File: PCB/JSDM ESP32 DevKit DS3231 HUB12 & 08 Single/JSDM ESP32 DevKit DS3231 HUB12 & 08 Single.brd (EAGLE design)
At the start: 14 parts, among them X1 PSU

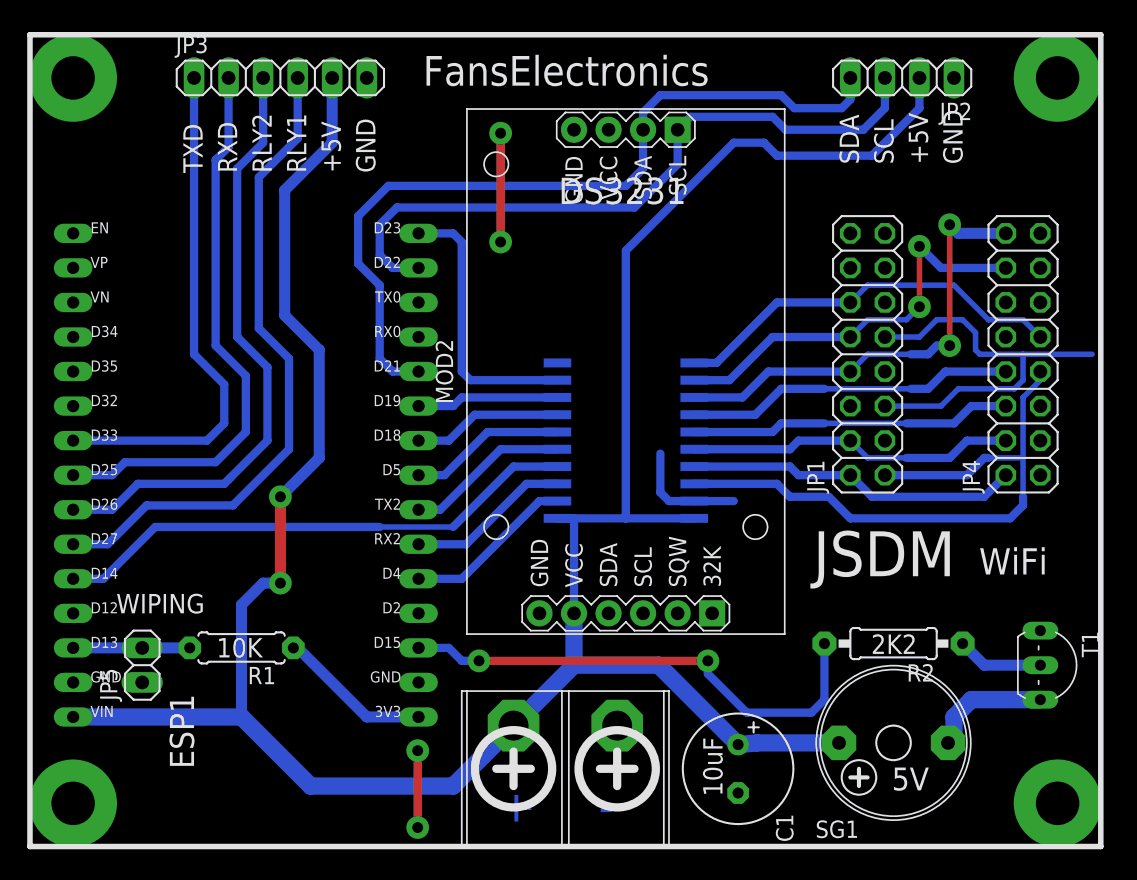
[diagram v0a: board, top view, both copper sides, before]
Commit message: JSDM PCB Single Layer ESP8266 + ESP32
Desain PCB SIngle Layer versi:
- Wemos D1 mini HUB12 + HUB08
- Wemos D1 Mini 3x HUB12
- ESP32 Devkit HUB12 + HUB08
- ESP32 Devkit Mini 3x HUB12
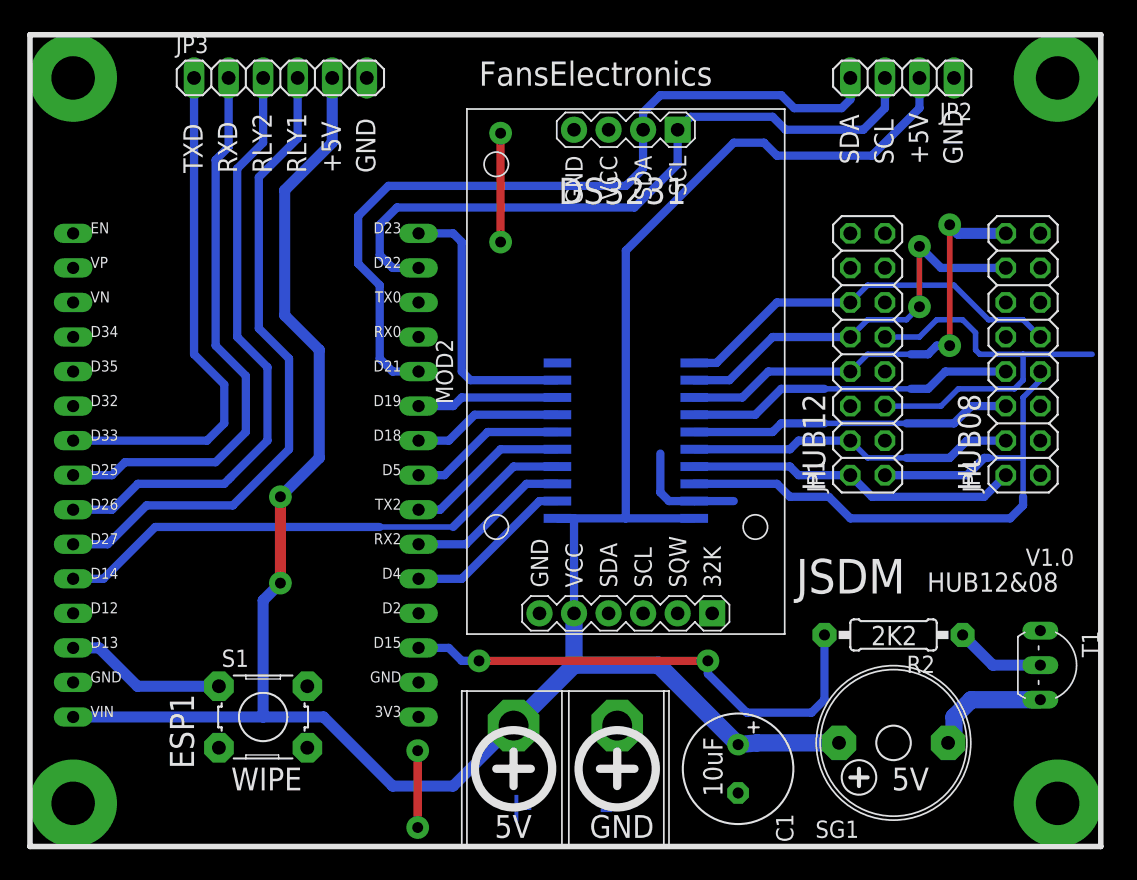
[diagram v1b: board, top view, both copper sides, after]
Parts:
- removed JP5: WIPE, FansElectronics-Header:1X02
- removed R1: 10K, FansElectronics-RCL:0207/7
- added S1: WIPE, FansElectronics-Switch:TACT-6X6MM-OCTAGON
- moved R2 0.63 mm to (90.8, 37.8)
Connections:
- removed net WIPING: ESP1.D13, JP5.2, R1.2
- new net WIPE: ESP1.D13, S1.1
- net +3V3: no longer R1.1
- net GND: now also S1.3, S1.4; no longer JP5.1
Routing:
- net WIPE: track 0.00 -> 11.9 mm
- net +3V3: track 11.0 -> 0.00 mm
- net WIPING: track 8.57 -> 0.00 mm
- net +5V: track 187.8 -> 186.4 mm
- net BUZZER: track 36.9 -> 37.5 mm
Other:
- board text added: "HUB08"
- board text added: "HUB12"
- board text added: "HUB12&08"
- board text added: "V1.0"
- board text added: "WIPE"
- board text removed: "10K"
- board text removed: "WIPING"
- board text removed: "WiFi"
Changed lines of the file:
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@@
 <setting verticaltext="up"/>
 </settings>
-<grid distance="0.0025" unitdist="inch" unit="inch" style="lines" multiple="1" display="no" altdistance="0.000125" altunitdist="inch" altunit="inch"/>
+<grid distance="0.05" unitdist="inch" unit="inch" style="lines" multiple="1" display="yes" altdistance="0.0125" altunitdist="inch" altunit="inch"/>
 <layers>
 <layer number="1" name="Top" color="4" fill="1" visible="yes" active="yes"/>
@@
 <wire x1="106.045" y1="22.225" x2="27.305" y2="22.225" width="0.4064" layer="21"/>
 <wire x1="27.305" y1="22.225" x2="27.305" y2="81.915" width="0.4064" layer="21"/>
-<text x="84.8995" y="42.1005" size="3.302" layer="21" font="vector" ratio="20" rot="SR0">JSDM</text>
-<text x="97.0915" y="42.2275" size="1.9304" layer="21" font="vector" ratio="19" rot="SR0">WiFi</text>
+<text x="83.6295" y="40.8305" size="2.54" layer="21" font="vector" ratio="20" rot="SR0">JSDM</text>
+<text x="93.2815" y="40.9575" size="1.4224" layer="21" font="vector" ratio="15" rot="SR0">HUB12&amp;08</text>
 <text x="64.16675" y="26.3525" size="2.54" layer="16" font="vector" ratio="21" rot="SMR270">+</text>
 <text x="69.11975" y="26.4795" size="2.54" layer="16" font="vector" ratio="21" rot="MR180">-</text>
 <text x="90.678" y="26.3525" size="1.6764" layer="21" font="vector" ratio="14" rot="SR0">5V</text>
 <text x="78.232" y="25.908" size="1.4224" layer="21" font="vector" ratio="14" rot="SR90">10uF</text>
-<text x="89.154" y="36.3855" size="1.4224" layer="21" font="vector" ratio="14">2K2</text>
+<text x="89.154" y="37.0205" size="1.4224" layer="21" font="vector" ratio="14">2K2</text>
 <text x="95.885" y="72.39" size="1.4224" layer="21" font="vector" ratio="14" rot="SR90">GND</text>
 <text x="93.345" y="72.39" size="1.4224" layer="21" font="vector" ratio="14" rot="SR90">+5V</text>
@@
 <text x="50.165" y="71.755" size="1.4224" layer="21" font="vector" ratio="14" rot="SR90">+5V</text>
 <text x="52.705" y="71.755" size="1.4224" layer="21" font="vector" ratio="14" rot="SR90">GND</text>
-<text x="33.655" y="39.37" size="1.4224" layer="21" font="vector" ratio="14" rot="SR0">WIPING</text>
-<text x="41.021" y="36.1315" size="1.4224" layer="21" font="vector" ratio="14">10K</text>
 <text x="66.167" y="69.469" size="1.9304" layer="21" font="vector" ratio="14" rot="SR0">DS3231</text>
-<text x="56.1975" y="78.1685" size="2.1844" layer="21" font="vector" ratio="18">FansElectronics</text>
+<text x="60.325" y="78.1685" size="1.778" layer="21" font="vector" ratio="15">FansElectronics</text>
+<text x="85.7885" y="48.387" size="1.6764" layer="21" font="vector" ratio="15" rot="SR90">HUB12</text>
+<text x="97.2185" y="48.387" size="1.6764" layer="21" font="vector" ratio="15" rot="SR90">HUB08</text>
+<text x="61.468" y="22.86" size="1.6764" layer="21" font="vector" ratio="14" rot="SR0">5V</text>
+<text x="68.453" y="22.86" size="1.6764" layer="21" font="vector" ratio="14" rot="SR0">GND</text>
+<text x="42.1005" y="26.3525" size="1.6764" layer="21" font="vector" ratio="14" rot="SR0">WIPE</text>
+<text x="100.5205" y="42.8625" size="1.27" layer="21" font="vector" ratio="15" rot="SR0">V1.0</text>
 </plain>
 <attributes>
@@
 <element name="JP4" library="FansElectronics-Header" package="2X08" value="HUB08" x="100.33" y="58.42" rot="R90"/>
 <element name="MOD2" library="FansElectronics-Modul" package="RTC-DS3231-MIRROR" value="RTC-3231MIRROR" x="71.12" y="57.15" rot="R90"/>
-<element name="R2" library="FansElectronics-RCL" package="0207/10" value="1K" x="90.805" y="37.1475" rot="R180"/>
+<element name="R2" library="FansElectronics-RCL" package="0207/10" value="1K" x="90.805" y="37.7825" rot="R180"/>
 <element name="SG1" library="FansElectronics-Buzzer" package="5V" value="5V-PCB" x="90.805" y="29.845" rot="R180"/>
 <element name="T1" library="transistor" package="TO92-EBC" value="" x="102.87" y="35.56" rot="R270"/>
 <element name="X1" library="FansElectronics-Con-Screw" package="TB2" value="PSU" x="66.675" y="31.115"/>
 <element name="JP3" library="FansElectronics-Header" package="1X06" value="MUROTTAL" x="45.72" y="78.74"/>
-<element name="R1" library="FansElectronics-RCL" package="0207/7" value="10K" x="42.8625" y="36.83" rot="R180"/>
-<element name="JP5" library="FansElectronics-Header" package="1X02" value="WIPE" x="35.56" y="35.56" rot="R90"/>
+<element name="S1" library="FansElectronics-Switch" package="TACT-6X6MM-OCTAGON" value="WIPE" x="44.45" y="31.75"/>
 </elements>
 <signals>
@@
 <contactref element="ESP1" pad="GND@1"/>
 <contactref element="ESP1" pad="GND@2"/>
-<contactref element="JP5" pad="1"/>
 <via x="55.8165" y="29.2735" extent="1-16" drill="0.8" diameter="1.6764" shape="octagon"/>
 <via x="55.8165" y="23.622" extent="1-16" drill="0.8" diameter="1.6764" shape="octagon"/>
@@
 <wire x1="96.8375" y1="60.0075" x2="96.8375" y2="58.7375" width="0.4064" layer="16"/>
 <wire x1="96.8375" y1="58.7375" x2="97.155" y2="58.42" width="0.4064" layer="16"/>
+<contactref element="S1" pad="3"/>
+<contactref element="S1" pad="4"/>
 </signal>
 <signal name="DMD_NOE">
@@
 <contactref element="JP3" pad="5"/>
 <contactref element="ESP1" pad="VIN"/>
-<wire x1="58.42" y1="26.67" x2="47.9425" y2="26.67" width="1.27" layer="16"/>
-<wire x1="47.9425" y1="26.67" x2="42.8625" y2="31.75" width="1.27" layer="16"/>
-<wire x1="42.8625" y1="31.75" x2="30.48" y2="31.75" width="1.27" layer="16"/>
 <wire x1="67.31" y1="39.37" x2="67.31" y2="46.355" width="0.6096" layer="16"/>
 <wire x1="67.31" y1="46.355" x2="66.0908" y2="46.355" width="0.6096" layer="16"/>
@@
 <wire x1="67.31" y1="39.37" x2="67.31" y2="35.56" width="1.27" layer="16"/>
 <wire x1="67.31" y1="35.56" x2="62.865" y2="31.115" width="1.27" layer="16"/>
-<wire x1="62.865" y1="31.115" x2="58.42" y2="26.67" width="1.27" layer="16"/>
 <wire x1="67.31" y1="35.56" x2="73.533" y2="35.56" width="1.27" layer="16"/>
 <wire x1="73.533" y1="35.56" x2="79.375" y2="29.718" width="1.27" layer="16"/>
@@
 <wire x1="45.72" y1="47.9425" x2="45.72" y2="41.5925" width="0.8128" layer="1"/>
 <via x="45.72" y="41.5925" extent="1-16" drill="0.8" diameter="1.6764" shape="octagon"/>
-<wire x1="45.72" y1="41.5925" x2="44.45" y2="41.5925" width="0.8128" layer="16"/>
-<wire x1="44.45" y1="41.5925" x2="42.8625" y2="40.005" width="0.8128" layer="16"/>
-<wire x1="42.8625" y1="40.005" x2="42.8625" y2="31.75" width="0.8128" layer="16"/>
+<wire x1="45.72" y1="41.5925" x2="44.45" y2="40.3225" width="0.8128" layer="16"/>
+<wire x1="44.45" y1="40.3225" x2="44.45" y2="31.75" width="0.8128" layer="16"/>
+<wire x1="30.48" y1="31.75" x2="44.45" y2="31.75" width="0.8128" layer="16"/>
+<wire x1="44.45" y1="31.75" x2="48.895" y2="31.75" width="0.8128" layer="16"/>
+<wire x1="48.895" y1="31.75" x2="53.975" y2="26.67" width="0.8128" layer="16"/>
+<wire x1="53.975" y1="26.67" x2="58.42" y2="26.67" width="0.8128" layer="16"/>
+<wire x1="58.42" y1="26.67" x2="62.865" y2="31.115" width="0.8128" layer="16"/>
 </signal>
 <signal name="R1">
@@
 <contactref element="T1" pad="B"/>
 <contactref element="R2" pad="1"/>
-<wire x1="101.6" y1="35.56" x2="97.4725" y2="35.56" width="0.8128" layer="16"/>
-<wire x1="97.4725" y1="35.56" x2="95.885" y2="37.1475" width="0.8128" layer="16"/>
+<wire x1="101.6" y1="35.56" x2="98.1075" y2="35.56" width="0.8128" layer="16"/>
+<wire x1="98.1075" y1="35.56" x2="95.885" y2="37.7825" width="0.8128" layer="16"/>
 </signal>
 <signal name="STB">
@@
 <contactref element="R2" pad="2"/>
 <contactref element="ESP1" pad="D15"/>
-<wire x1="85.725" y1="37.1475" x2="85.725" y2="33.02" width="0.6096" layer="16"/>
+<wire x1="85.725" y1="37.7825" x2="85.725" y2="33.02" width="0.6096" layer="16"/>
 <wire x1="85.725" y1="33.02" x2="84.7725" y2="32.0675" width="0.6096" layer="16"/>
 <wire x1="84.7725" y1="32.0675" x2="80.01" y2="32.0675" width="0.6096" layer="16"/>
@@
 <wire x1="58.42" y1="67.31" x2="55.88" y2="67.31" width="0.6096" layer="16"/>
 </signal>
-<signal name="WIPING">
-<contactref element="JP5" pad="2"/>
-<contactref element="R1" pad="2"/>
+<signal name="+3V3">
+<contactref element="ESP1" pad="3V3"/>
+</signal>
+<signal name="WIPE">
 <contactref element="ESP1" pad="D13"/>
-<wire x1="39.0525" y1="36.83" x2="36.83" y2="36.83" width="0.8128" layer="16"/>
-<wire x1="36.83" y1="36.83" x2="35.56" y2="36.83" width="0.8128" layer="16"/>
-<wire x1="30.48" y1="36.83" x2="35.56" y2="36.83" width="0.8128" layer="16"/>
-</signal>
-<signal name="+3V3">
-<contactref element="R1" pad="1"/>
-<contactref element="ESP1" pad="3V3"/>
-<wire x1="55.88" y1="31.75" x2="52.07" y2="31.75" width="0.8128" layer="16"/>
-<wire x1="52.07" y1="31.75" x2="46.99" y2="36.83" width="0.8128" layer="16"/>
-<wire x1="46.99" y1="36.83" x2="46.6725" y2="36.83" width="0" layer="19" extent="16-16"/>
+<contactref element="S1" pad="1"/>
+<wire x1="41.1988" y1="34.0106" x2="35.2044" y2="34.0106" width="0.8128" layer="16"/>
+<wire x1="35.2044" y1="34.0106" x2="32.385" y2="36.83" width="0.8128" layer="16"/>
+<wire x1="32.385" y1="36.83" x2="30.48" y2="36.83" width="0.8128" layer="16"/>
 </signal>
 </signals>
